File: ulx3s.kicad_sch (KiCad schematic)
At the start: 4 parts

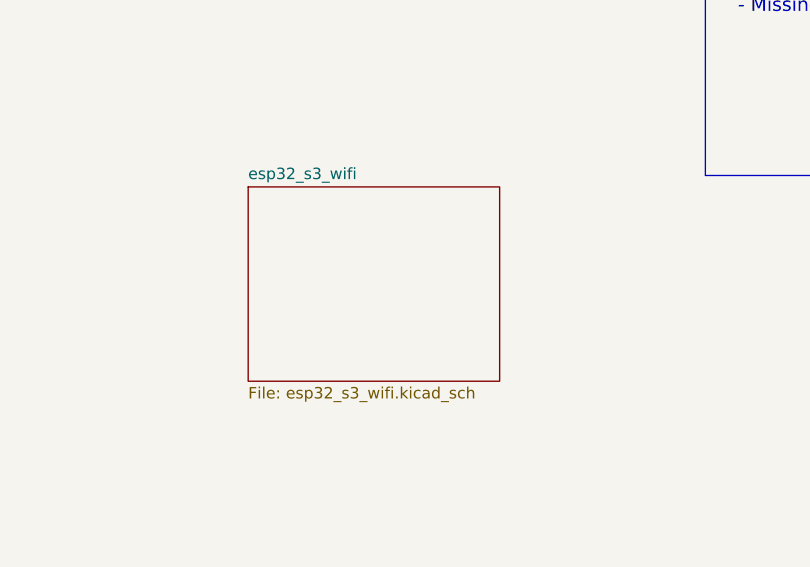
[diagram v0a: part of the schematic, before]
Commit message: remove extra schematic page for esp32
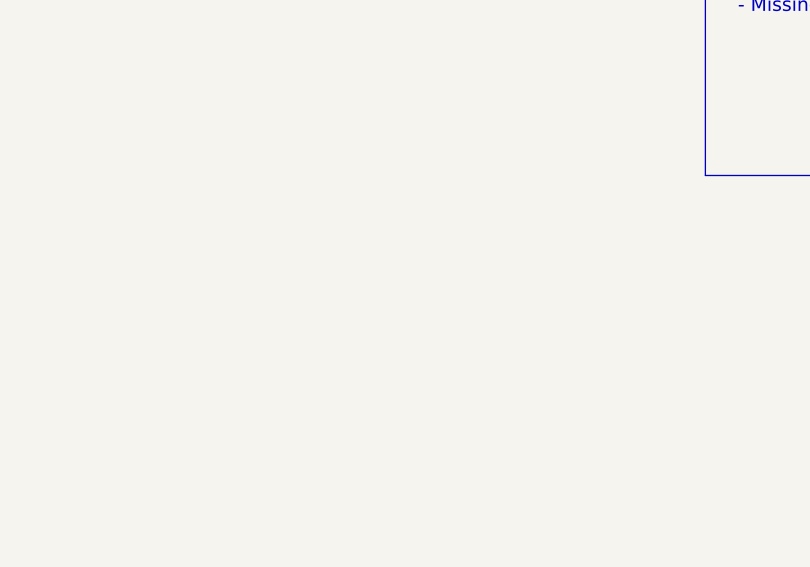
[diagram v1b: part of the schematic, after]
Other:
- removed sheet esp32_s3_wifi
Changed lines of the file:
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@@
-		)
-	)
-	(sheet
-		(at 102.87 93.98)
-		(size 27.94 21.59)
-		(exclude_from_sim no)
-		(in_bom yes)
-		(on_board yes)
-		(dnp no)
-		(fields_autoplaced yes)
-		(stroke
-			(width 0.1524)
-			(type solid)
-		)
-		(fill
-			(color 0 0 0 0)
-		)
-		(property "Sheetname" "esp32_s3_wifi"
-			(at 102.87 93.2684 0)
-			(show_name no)
-			(do_not_autoplace no)
-			(effects
-				(font
-					(size 1.27 1.27)
-				)
-				(justify left bottom)
-			)
-		)
-		(property "Sheetfile" "esp32_s3_wifi.kicad_sch"
-			(at 102.87 116.1546 0)
-			(show_name no)
-			(do_not_autoplace no)
-			(effects
-				(font
-					(size 1.27 1.27)
-				)
-				(justify left top)
-			)
-		)
-		(instances
-			(project "ulx3s"
-				(path "/49a43414-f3c1-43b2-ad20-ac3166075f21"
-					(page "13")
-				)
-			)
 		)
 	)

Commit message: reposition flash to bottom. route esp32-s3. fix drc issues
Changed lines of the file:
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@@
 		)
 	)
-	(text_box "0.0.6 - build\ncurrent\n	- Marked RV2 as DNP - Stencil Issue\n	- VJ1/RP1/RP2/RP3/J1/J2/D51/D52/D9/J4/J6/H1/H2/H3/H4 marked as DNP - doesn't affect stencil\n	- Missing RV3 0ohm resistor"
+	(text_box "0.0.6 - build (fab'd)\ncurrent\n	- Marked RV2 as DNP - Stencil Issue\n	- VJ1/RP1/RP2/RP3/J1/J2/D51/D52/D9/J4/J6/H1/H2/H3/H4 marked as DNP - doesn't affect stencil\n	- Missing RV3 0ohm resistor\n0.0.7-alpha1 - (not fab'd)\n	- found OLED_BL/J4 (fixed)\n	- 		SD_WP/P5 still \"connected\" (fixed)"
 		(exclude_from_sim no)
 		(at 153.67 57.15 0)

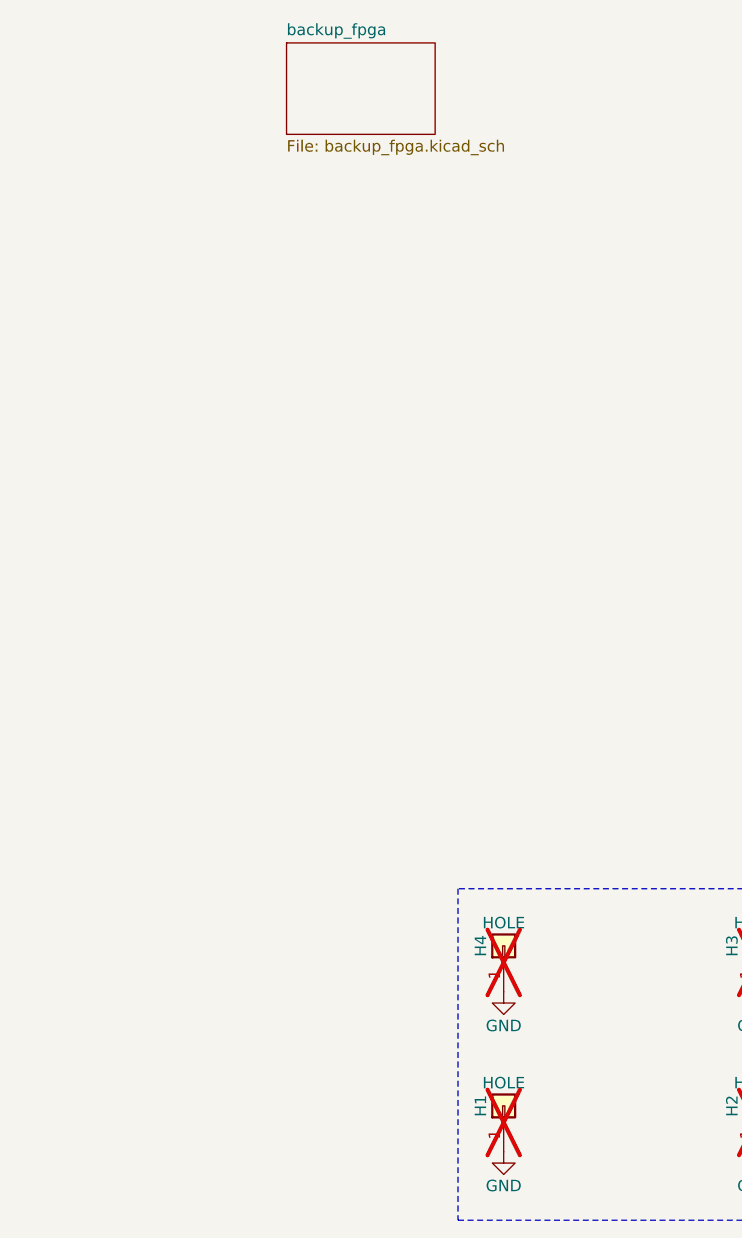
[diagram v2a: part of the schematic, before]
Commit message: remove extra sheet for alt fpga
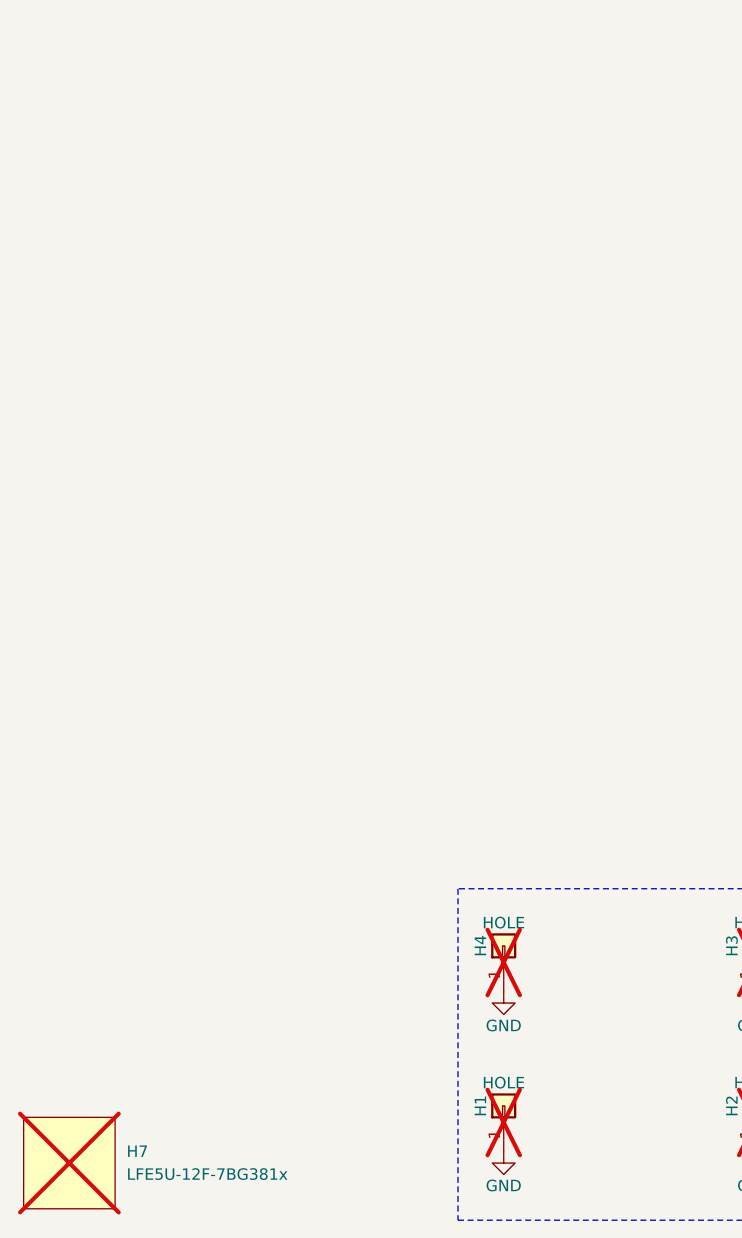
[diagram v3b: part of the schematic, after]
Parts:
- added H7: LFE5U-12F-7BG381x, Package_BGA:Lattice_caBGA-381_17x17mm_Layout20x20_P0.8mm, symbol Auxiliary_Items:Generic_Outline
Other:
- removed sheet backup_fpga
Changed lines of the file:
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@@
+		)
+	)
+	(symbol
+		(lib_id "Auxiliary_Items:Generic_Outline")
+		(at 31.75 167.64 0)
+		(unit 1)
+		(body_style 1)
+		(exclude_from_sim yes)
+		(in_bom yes)
+		(on_board no)
+		(in_pos_files no)
+		(dnp yes)
+		(fields_autoplaced yes)
+		(property "Reference" "H7"
+			(at 38.1 166.3699 0)
+			(show_name no)
+			(do_not_autoplace no)
+			(effects
+				(font
+					(size 1.27 1.27)
+				)
+				(justify left)
+			)
+		)
+		(property "Value" "LFE5U-12F-7BG381x"
+			(at 38.1 168.9099 0)
+			(show_name no)
+			(do_not_autoplace no)
+			(effects
+				(font
+					(size 1.27 1.27)
+				)
+				(justify left)
+			)
+		)
+		(property "Footprint" "Package_BGA:Lattice_caBGA-381_17x17mm_Layout20x20_P0.8mm"
+			(at 43.18 95.25 0)
+			(hide yes)
+			(show_name no)
+			(do_not_autoplace no)
+			(effects
+				(font
+					(size 1.27 1.27)
+				)
+			)
+		)
+		(property "Datasheet" "https://www.latticesemi.com/view_document?document_id=50461"
+			(at 43.18 95.25 0)
+			(hide yes)
+			(show_name no)
+			(do_not_autoplace no)
+			(effects
+				(font
+					(size 1.27 1.27)
+				)
+			)
+		)
+		(property "Description" "ECP5 FPGA, 12K LUTs, 1.2V, BGA-381"
+			(at 31.75 167.64 0)
+			(hide yes)
+			(show_name no)
+			(do_not_autoplace no)
+			(effects
+				(font
+					(size 1.27 1.27)
+				)
+			)
+		)
+		(property "Field5" ""
+			(at 31.75 167.64 0)
+			(hide yes)
+			(show_name no)
+			(do_not_autoplace no)
+			(effects
+				(font
+					(size 1.524 1.524)
+				)
+			)
+		)
+		(property "Digikey" "220-2101-ND"
+			(at 31.75 167.64 0)
+			(hide yes)
+			(show_name no)
+			(do_not_autoplace no)
+			(effects
+				(font
+					(size 1.524 1.524)
+				)
+			)
+		)
+		(property "MPN" "842-LFE5U12F7BG381C"
+			(at 31.75 167.64 0)
+			(hide yes)
+			(show_name no)
+			(do_not_autoplace no)
+			(effects
+				(font
+					(size 1.27 1.27)
+				)
+			)
+		)
+		(property "Arrow" ""
+			(at 31.75 167.64 0)
+			(hide yes)
+			(show_name no)
+			(do_not_autoplace no)
+			(effects
+				(font
+					(size 1.524 1.524)
+				)
+			)
+		)
+		(property "DatasheetLC" ""
+			(at 31.75 167.64 0)
+			(hide yes)
+			(show_name no)
+			(do_not_autoplace no)
+			(effects
+				(font
+					(size 1.524 1.524)
+				)
+			)
+		)
+		(property "LCS_C2" ""
+			(at 31.75 167.64 0)
+			(hide yes)
+			(show_name no)
+			(do_not_autoplace no)
+			(effects
+				(font
+					(size 1.524 1.524)
+				)
+			)
+		)
+		(property "MP_N4" ""
+			(at 31.75 167.64 0)
+			(hide yes)
+			(show_name no)
+			(do_not_autoplace no)
+			(effects
+				(font
+					(size 1.524 1.524)
+				)
+			)
+		)
+		(property "MP_N5" ""
+			(at 31.75 167.64 0)
+			(hide yes)
+			(show_name no)
+			(do_not_autoplace no)
+			(effects
+				(font
+					(size 1.524 1.524)
+				)
+			)
+		)
+		(property "Vertical" ""
+			(at 31.75 167.64 0)
+			(hide yes)
+			(show_name no)
+			(do_not_autoplace no)
+			(effects
+				(font
+					(size 1.524 1.524)
+				)
+			)
+		)
+		(property "price100_Mouser" ""
+			(at 31.75 167.64 0)
+			(hide yes)
+			(show_name no)
+			(do_not_autoplace no)
+			(effects
+				(font
+					(size 1.524 1.524)
+				)
+			)
+		)
+		(property "price1200_Chip1stop" ""
+			(at 31.75 167.64 0)
+			(hide yes)
+			(show_name no)
+			(do_not_autoplace no)
+			(effects
+				(font
+					(size 1.524 1.524)
+				)
+			)
+		)
+		(property "price300_LCSC" ""
+			(at 31.75 167.64 0)
+			(hide yes)
+			(show_name no)
+			(do_not_autoplace no)
+			(effects
+				(font
+					(size 1.524 1.524)
+				)
+			)
+		)
+		(property "price300_Vertical" ""
+			(at 31.75 167.64 0)
+			(hide yes)
+			(show_name no)
+			(do_not_autoplace no)
+			(effects
+				(font
+					(size 1.524 1.524)
+				)
+			)
+		)
+		(property "price_Arrow" ""
+			(at 31.75 167.64 0)
+			(hide yes)
+			(show_name no)
+			(do_not_autoplace no)
+			(effects
+				(font
+					(size 1.524 1.524)
+				)
+			)
+		)
+		(instances
+			(project "ulx3s"
+				(path "/49a43414-f3c1-43b2-ad20-ac3166075f21"
+					(reference "H7")
+					(unit 1)
+				)
+			)
 		)
 	)
@@
 				)
 			)
-		)
-	)
-	(sheet
-		(at 55.88 43.18)
-		(size 16.51 10.16)
-		(exclude_from_sim no)
-		(in_bom yes)
-		(on_board yes)
-		(dnp no)
-		(fields_autoplaced yes)
-		(stroke
-			(width 0.1524)
-			(type solid)
-		)
-		(fill
-			(color 0 0 0 0)
-		)
-		(property "Sheetname" "backup_fpga"
-			(at 55.88 42.4684 0)
-			(show_name no)
-			(do_not_autoplace no)
-			(effects
-				(font
-					(size 1.27 1.27)
-				)
-				(justify left bottom)
-			)
-		)
-		(property "Sheetfile" "backup_fpga.kicad_sch"
-			(at 55.88 53.9246 0)
-			(show_name no)
-			(do_not_autoplace no)
-			(effects
-				(font
-					(size 1.27 1.27)
-				)
-				(justify left top)
-			)
-		)
-		(instances
-			(project "ulx3s"
-				(path "/49a43414-f3c1-43b2-ad20-ac3166075f21"
-					(page "12")
-				)
-			)

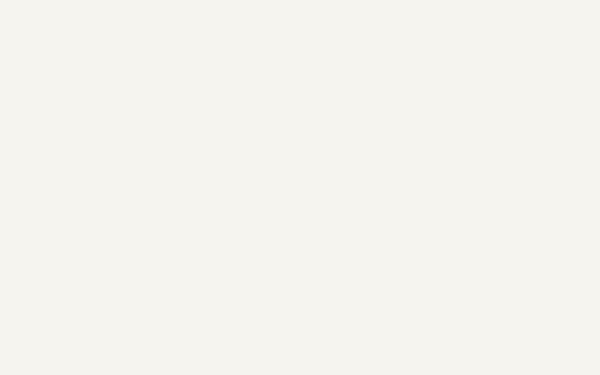
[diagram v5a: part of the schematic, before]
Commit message: move to v1.0.2 - use 0.09mm default trace
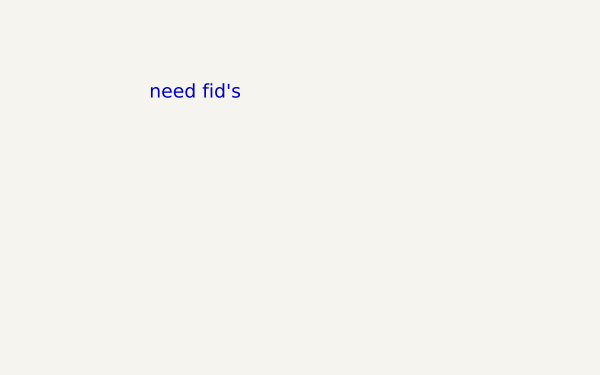
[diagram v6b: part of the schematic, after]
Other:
- note added: "need fid's"
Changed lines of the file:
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@@
 		(comment 1 "Root sheet")
+	)
+	(text "need fid's"
+		(exclude_from_sim no)
+		(at 45.72 65.532 0)
+		(effects
+			(font
+				(size 1.524 1.524)
+			)
+		)
 	)
 	(text "click on mouse pointer arrow on top of right toolbar\nand double-click on sheet to open"

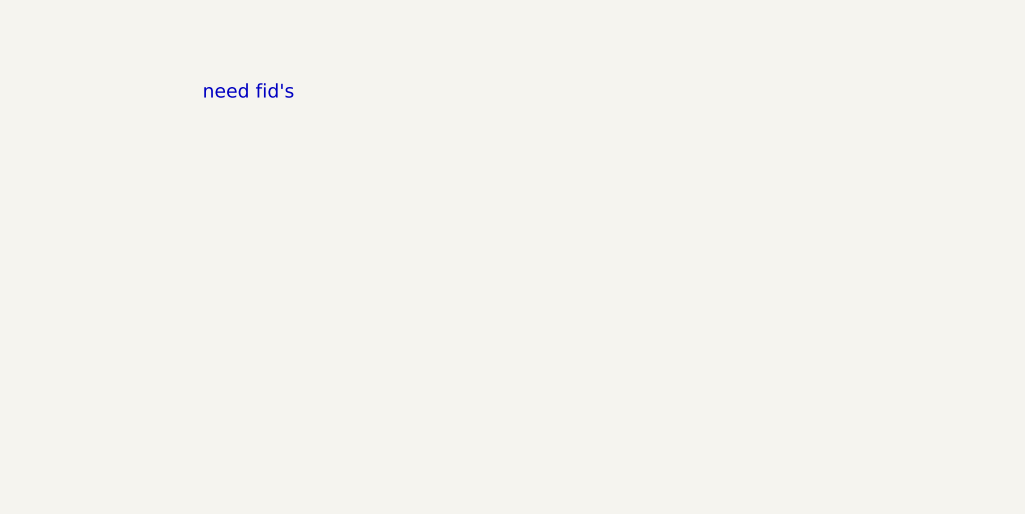
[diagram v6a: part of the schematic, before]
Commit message: update board stackup
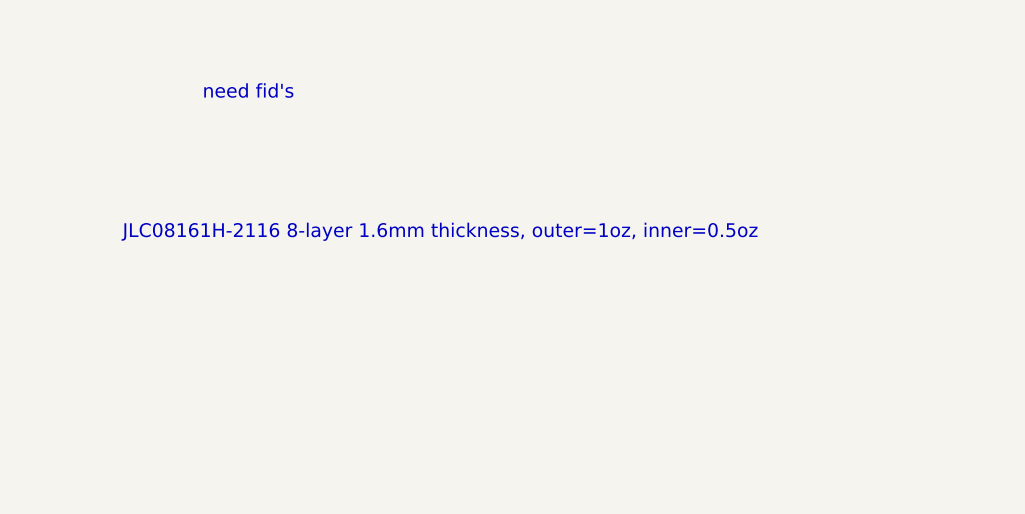
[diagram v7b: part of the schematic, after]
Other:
- note added: "JLC08161H-2116 8-layer 1.6mm thickness, outer=1oz, inner=0.5oz"
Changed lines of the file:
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@@
+		)
+	)
+	(text "JLC08161H-2116 8-layer 1.6mm thickness, outer=1oz, inner=0.5oz"
+		(exclude_from_sim no)
+		(at 67.056 81.026 0)
+		(effects
+			(font
+				(size 1.524 1.524)
+			)
 		)
 	)

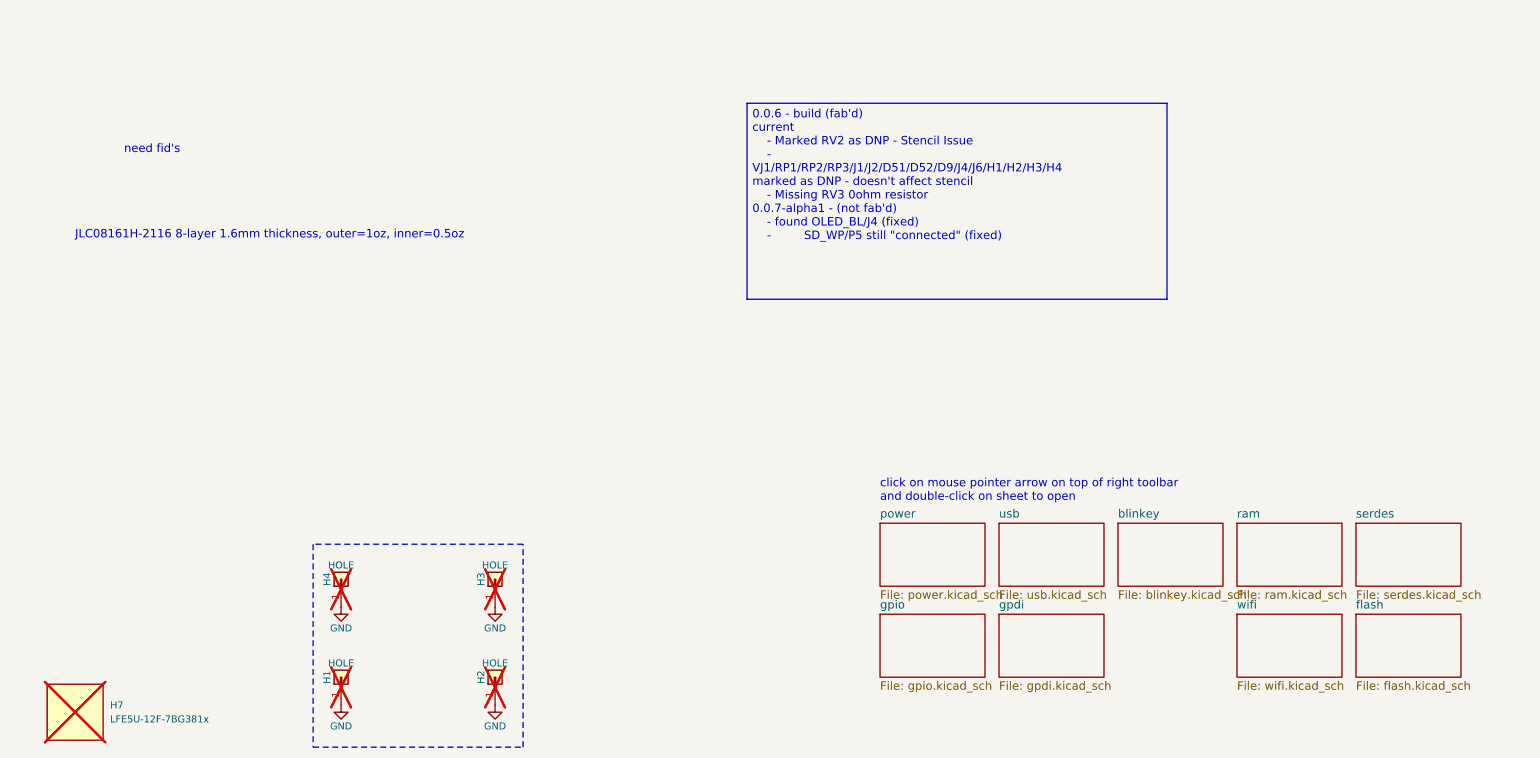
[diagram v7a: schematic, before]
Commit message: add fids, add attributions on board, bump to v1.0.5
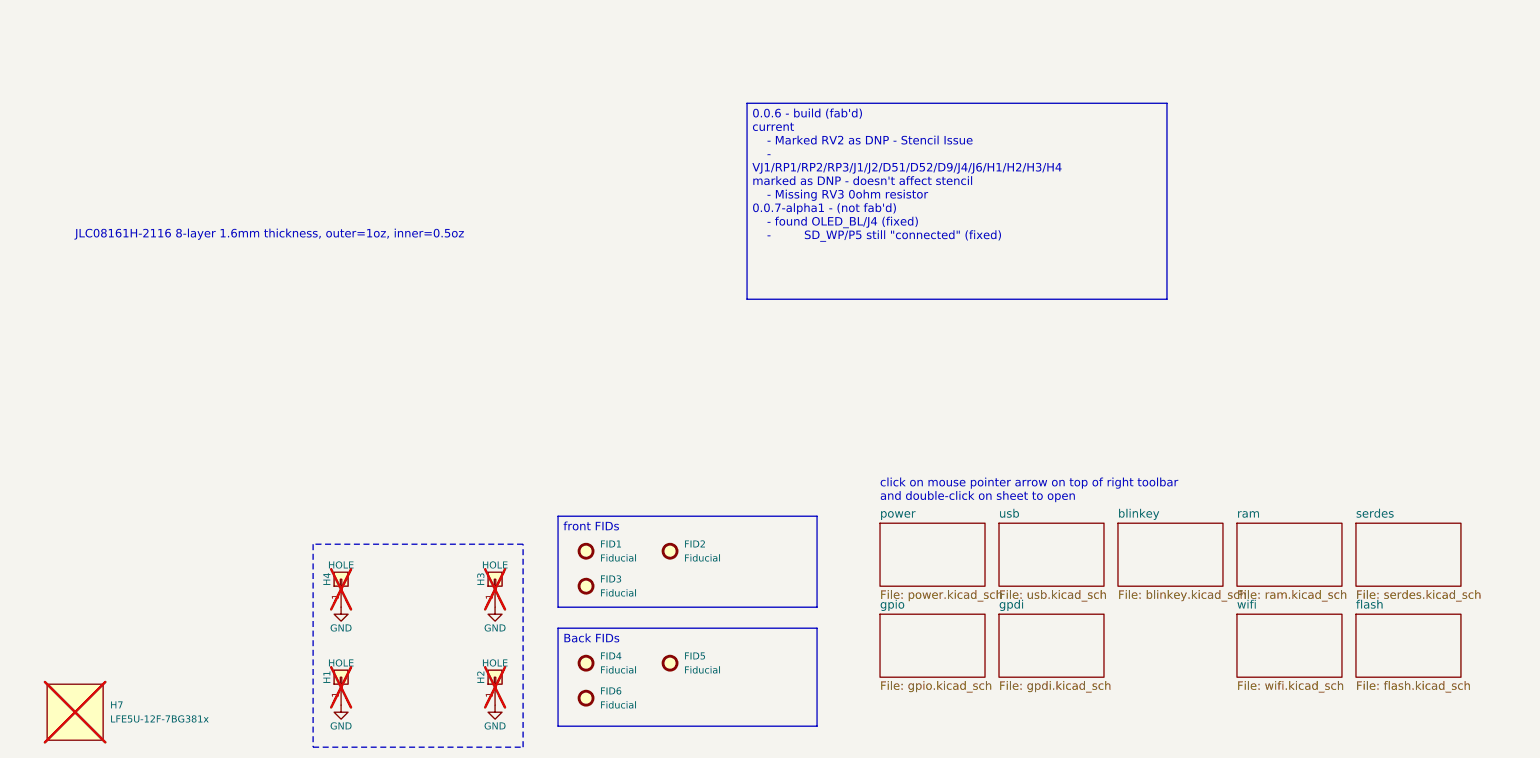
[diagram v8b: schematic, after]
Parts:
- added FID1, FID2, FID3, FID4, FID5, FID6: Fiducial, Fiducial:Fiducial_0.5mm_Mask1mm, symbol Mechanical:Fiducial
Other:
- note removed: "need fid's"
